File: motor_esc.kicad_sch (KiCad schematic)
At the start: 0 parts

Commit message: imu, motor esc schematics
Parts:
- added C10, C16: 22uF, Capacitor_SMD:C_1206_3216Metric_Pad1.33x1.80mm_HandSolder, symbol Device:C_Small
- added C11: 100nF, Capacitor_SMD:C_0603_1608Metric_Pad1.08x0.95mm_HandSolder, symbol Device:C_Small
- added C12: 47nF, Capacitor_SMD:C_0603_1608Metric_Pad1.08x0.95mm_HandSolder, symbol Device:C_Small
- added C13, C14, C15: 1uF, Capacitor_SMD:C_0603_1608Metric_Pad1.08x0.95mm_HandSolder, symbol Device:C_Small
- added L1: 2.2uH, Inductor_SMD:L_1008_2520Metric_Pad1.43x2.20mm_HandSolder, symbol Device:L_Ferrite_Small
- added U3: MCF8316A, symbol MCF8316A:MCF8316A
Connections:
- new net: L1.1, U3.5 (SW_BK)
- new net: C12.1, U3.7 (CPH)
- new net: C12.2, U3.6 (CPL)
- new net: C15.1, U3.1 (DVDD)
- new net: C15.2, U3.2 (DGND)
- new net: C14.2, U3.26 (AGND)
- new net: C14.1, U3.27 (AVDD)
- new net: C13.1, U3.8 (CP)
- new net GND_BK_M1: C16.2, U3.4 (GND_BK)
- new net M1_A: U3.13 (OUTA), U3.14 (OUTA)
- new net M1_B: U3.16 (OUTB), U3.17 (OUTB)
- new net M1_C: U3.19 (OUTC), U3.20 (OUTC)
- new net PGND_M1: C10.1, C11.2, U3.12 (PGND), U3.15 (PGND), U3.18 (PGND), U3.41 (EP)
- new net VBAT: C10.2, C11.1, C13.2, U3.10 (VM), U3.11 (VM), U3.9 (VM)
- new net VBK_M1: C16.1, L1.2, U3.3 (FB_BK)

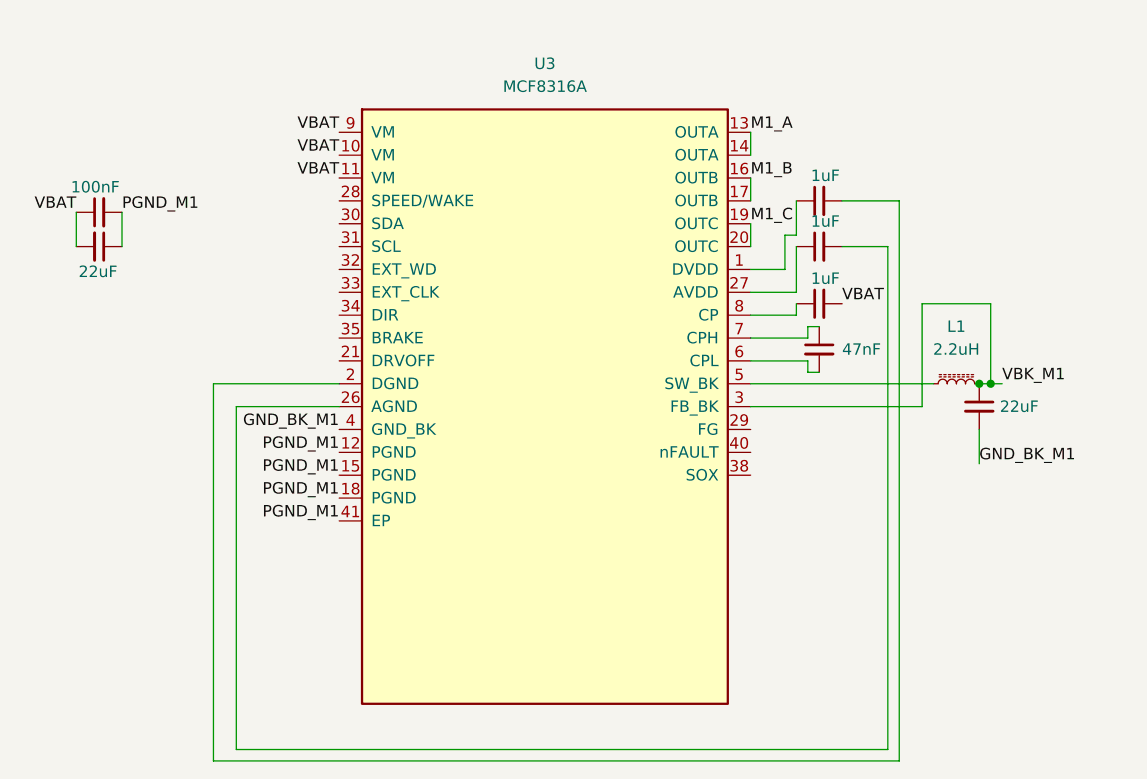
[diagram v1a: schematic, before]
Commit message: more esc schematics, refactoring, root schematic edits
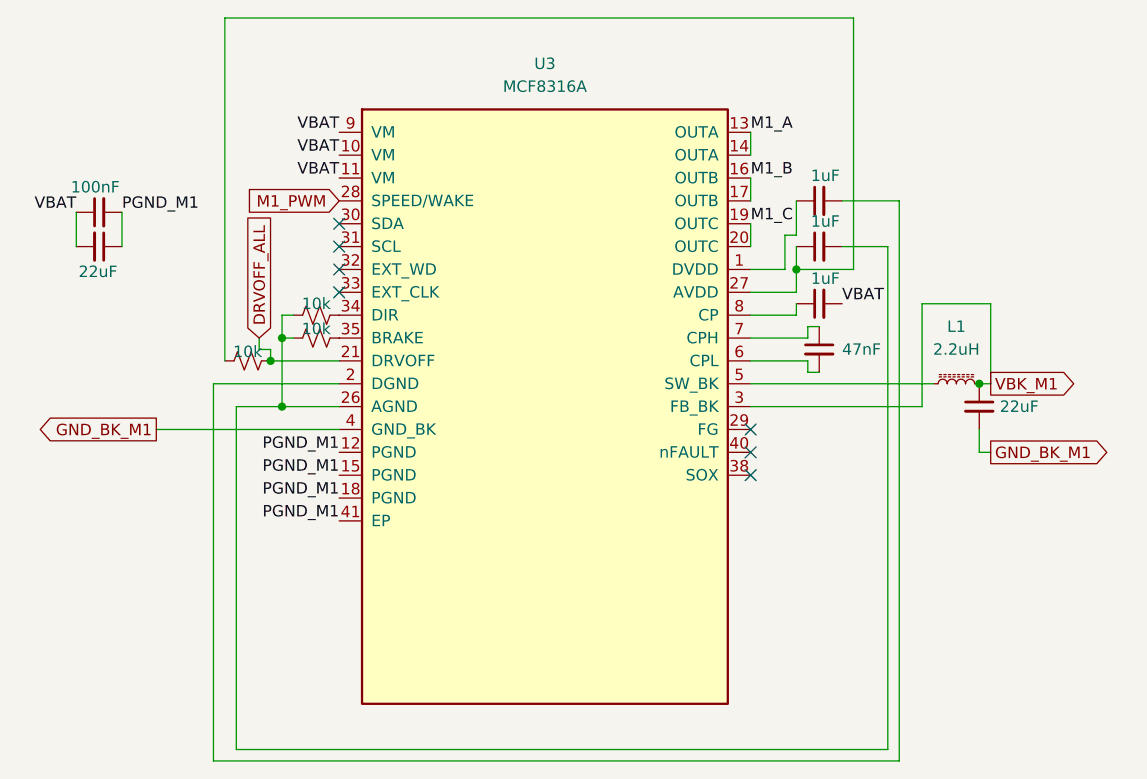
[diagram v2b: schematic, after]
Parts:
- added R4, R5, R6: 10k, Resistor_SMD:R_0603_1608Metric_Pad0.98x0.95mm_HandSolder, symbol Device:R_Small_US
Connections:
- net DRVOFF_ALL: now reaches U3.21 (DRVOFF)
- net DRVOFF_ALL: now also R6.2
- net at C14.2, U3.26 (AGND): now also R4.1, R5.1
- net at C14.1, U3.27 (AVDD): now also R6.1
- net M1_PWM: now reaches U3.28 (SPEED/WAKE)
- net at U3.34 (DIR): now also R4.2
- net at U3.35 (BRAKE): now also R5.2
- no-connect marks 0 -> 7
